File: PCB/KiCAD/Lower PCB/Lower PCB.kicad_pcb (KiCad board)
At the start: 2 copper layers, 188.6 x 165.4 mm, 106 parts, among them IC1 ADG608BRZ, IC2 ADG608BRZ, IC3 ADG608BRZ, J1 Conn_01x02_MountingPin, J2 Conn_01x04_MountingPin, J3 Conn_01x04_MountingPin, J4 Conn_01x04_MountingPin, Q1 SFH320, Q10 SFH320, Q11 SFH320, Q12 SFH320, Q13 SFH320, Q14 SFH320, Q15 SFH320, Q16 SFH320, Q17 SFH320, Q18 SFH320, Q19 SFH320, Q2 SFH320, Q20 SFH320, Q21 SFH320, Q22 SFH320, Q23 SFH320, Q24 SFH320, Q3 SFH320, Q4 SFH320, Q5 SFH320, Q6 SFH320, Q7 SFH320, Q8 SFH320, Q9 SFH320

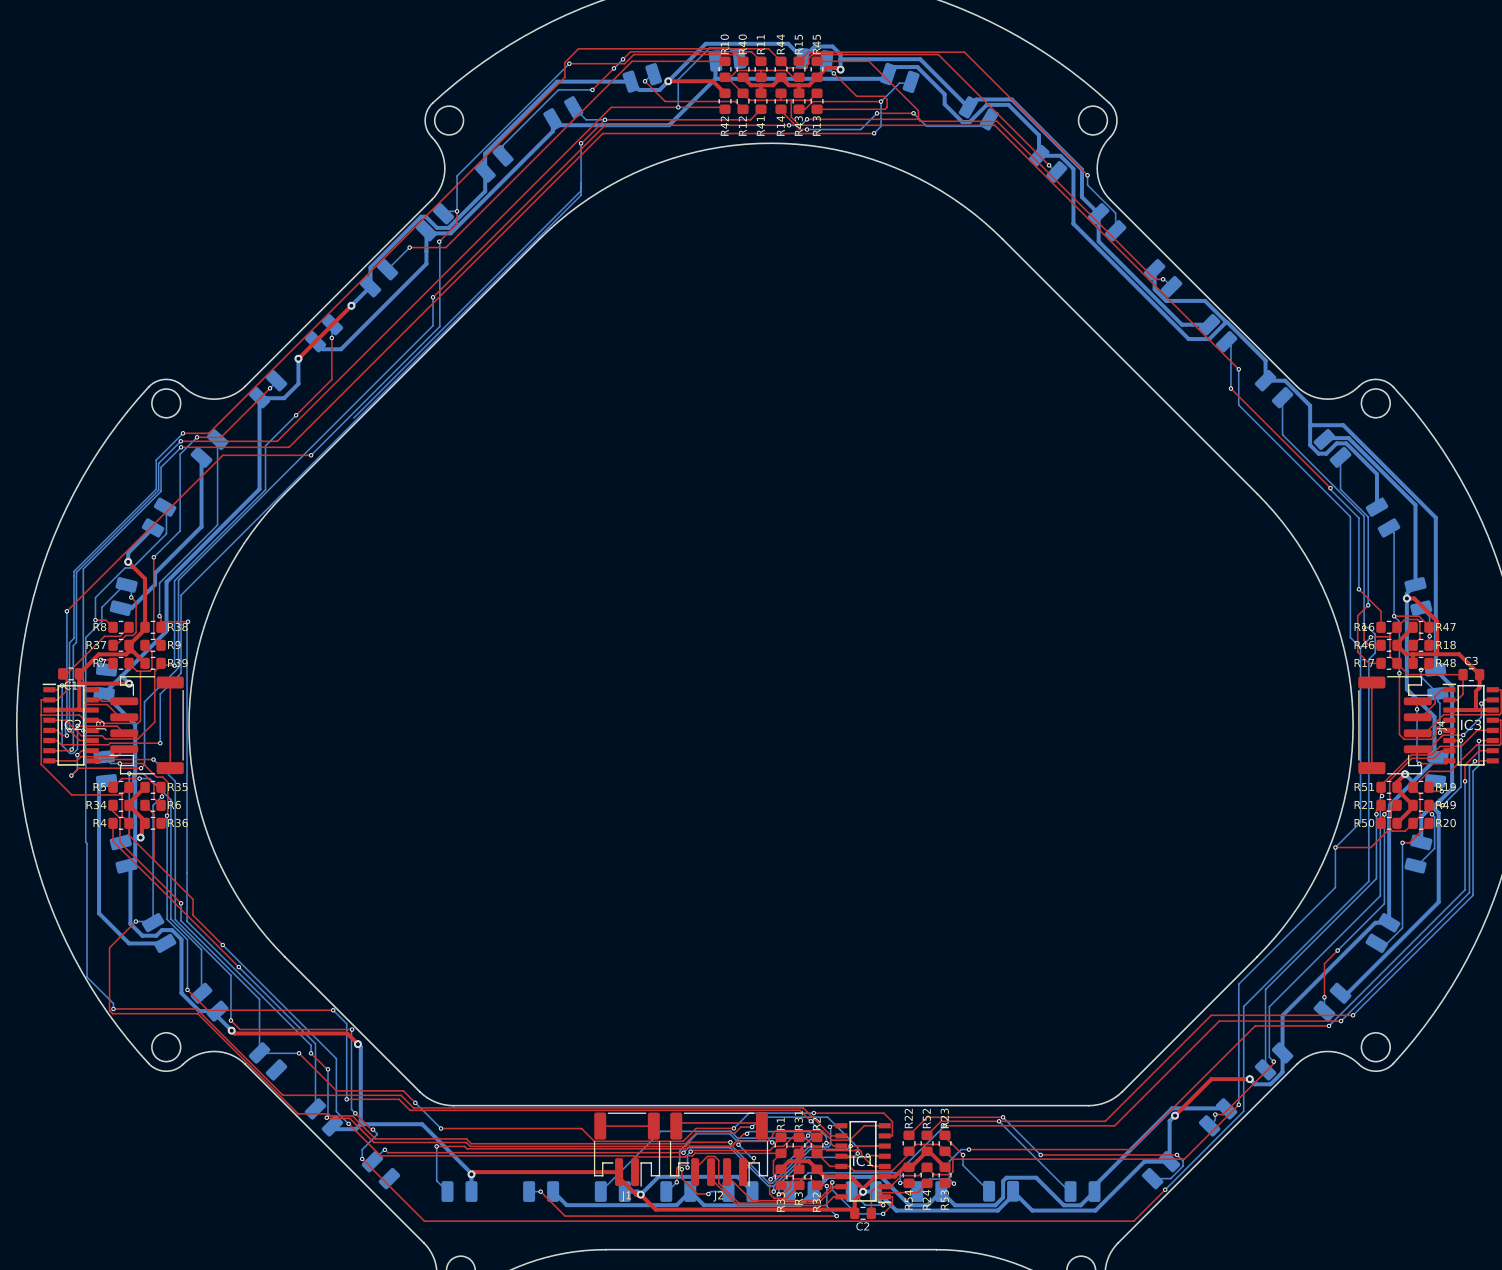
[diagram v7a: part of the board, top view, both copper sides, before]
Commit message: Lower PCb fully traced
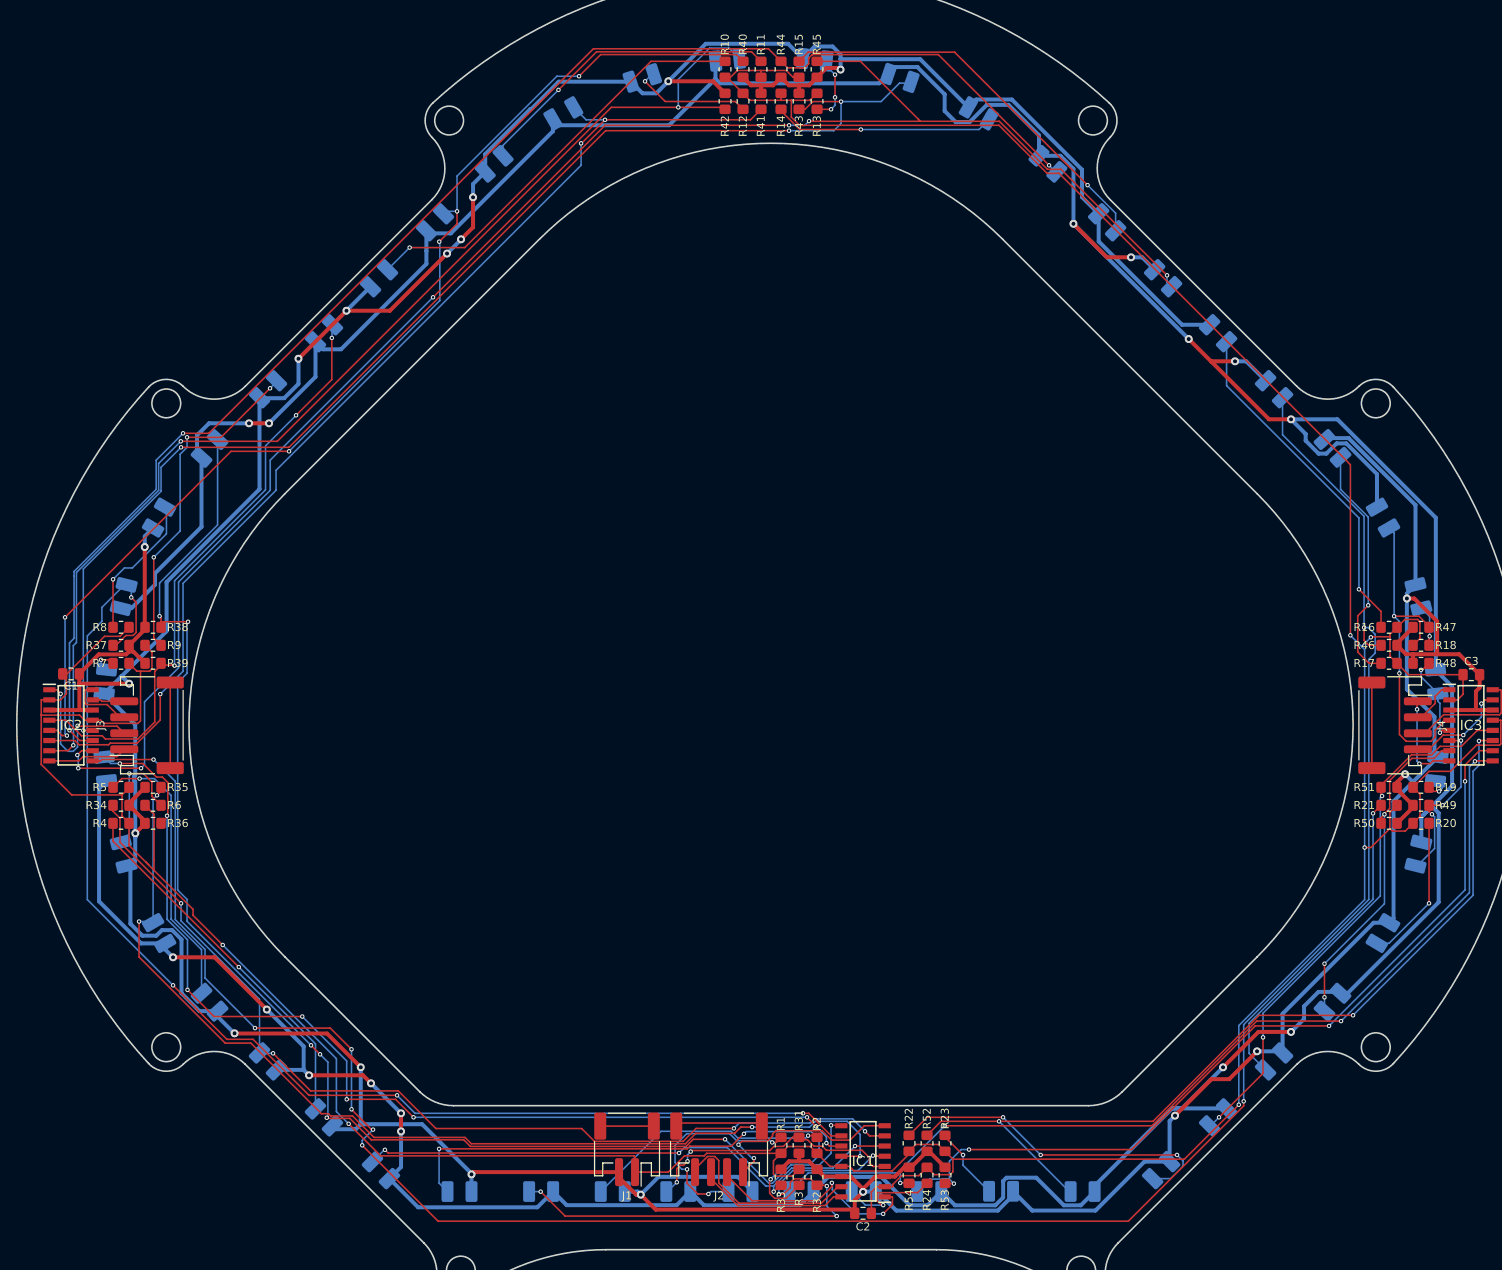
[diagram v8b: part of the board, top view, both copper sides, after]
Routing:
- net +5V: track 452.1 -> 587.0 mm, vias 0 -> 15
- net Net-(IC2-S3): track 180.9 -> 138.1 mm
- net Net-(D13-A): track 19.8 -> 8.44 mm, vias 1 -> 3
- net Net-(IC1-S5): track 138.4 -> 130.3 mm
- net Net-(IC1-S7): track 164.4 -> 158.0 mm, vias 2 -> 4
- net Net-(IC2-S5): track 164.3 -> 159.1 mm
- net Net-(IC2-S8): track 302.5 -> 297.9 mm
- net Net-(IC1-S4): track 126.9 -> 123.3 mm, vias 6 -> 4
- net Net-(IC1-S6): track 133.4 -> 130.6 mm, vias 7 -> 9
- net Net-(D8-A): track 21.0 -> 18.4 mm
- net Net-(IC2-S7): track 214.6 -> 212.2 mm
- net Net-(IC2-S2): track 143.5 -> 141.3 mm
- net Net-(D3-A): track 68.5 -> 70.3 mm
- net Net-(D21-A): track 39.1 -> 40.8 mm
- net Net-(D1-A): track 24.6 -> 26.2 mm
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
